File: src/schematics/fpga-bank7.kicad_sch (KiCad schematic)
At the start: 7 parts

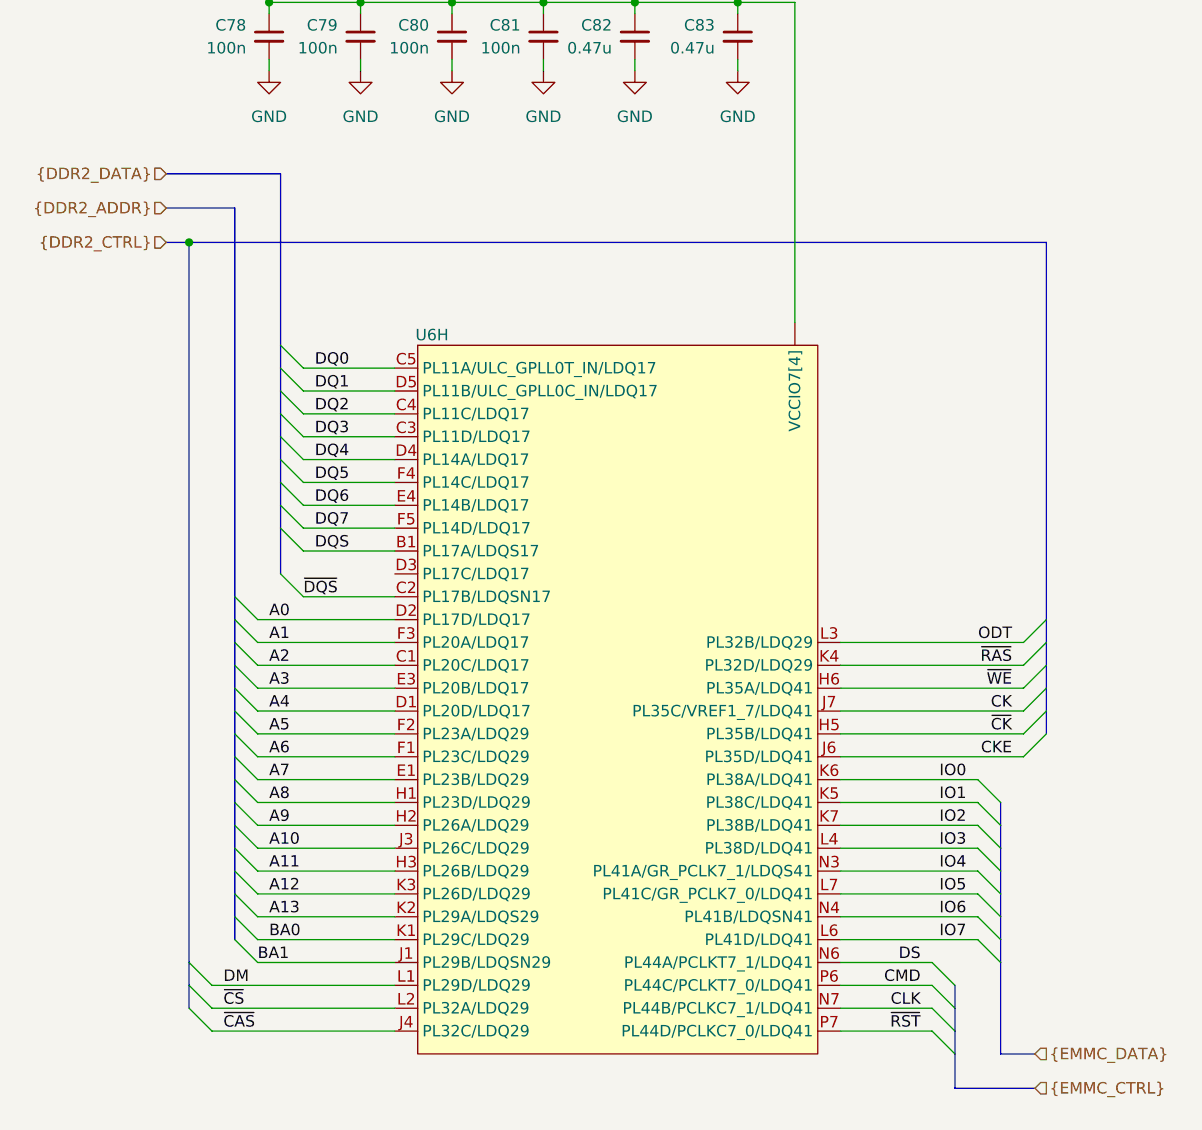
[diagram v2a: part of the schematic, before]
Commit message: Adds bus aliases
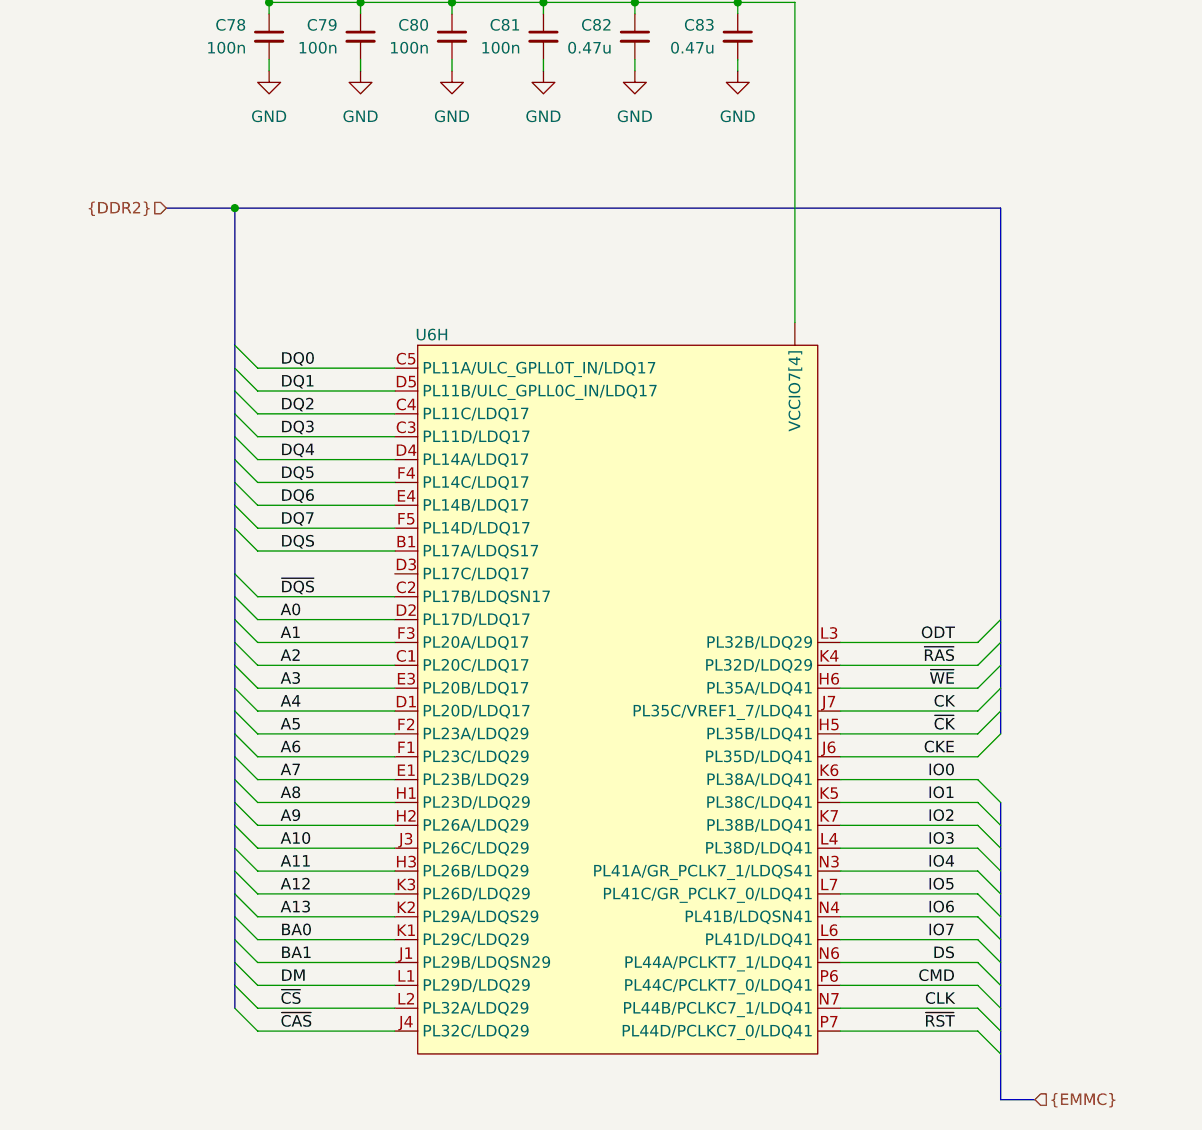
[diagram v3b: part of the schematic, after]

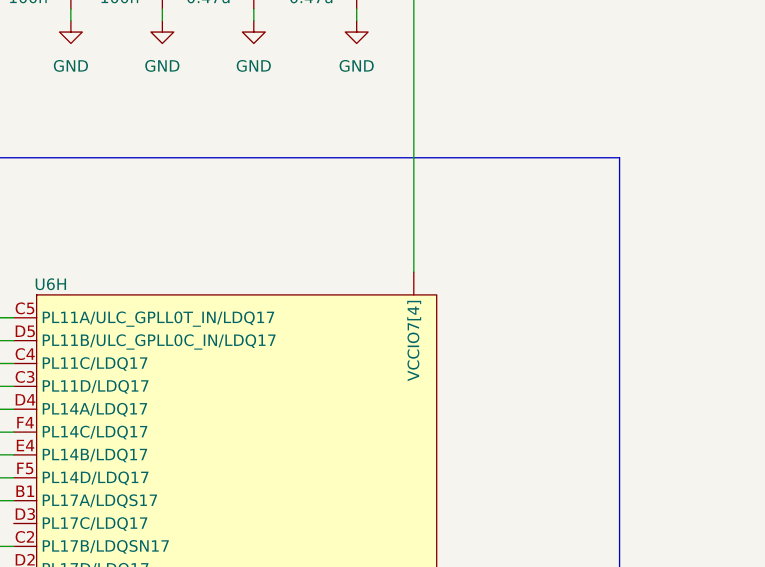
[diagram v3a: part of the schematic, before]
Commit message: Fix some ERC issues
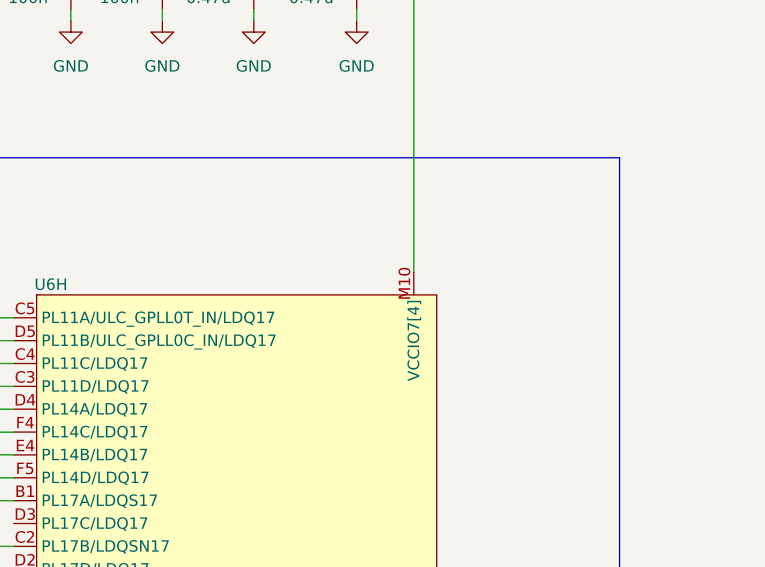
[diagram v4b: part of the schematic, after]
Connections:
- net +1V8: no longer U6. (VCCIO7[4])
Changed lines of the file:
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@@
 		(pin "Y31"
 		)
-		(pin ""
-		)
 		(pin "A10"
 		)
@@
 		(pin "Y32"
 		)
-		(pin ""
-		)
 		(pin "AB23"
 		)
@@
 		(pin "K16"
 		)
-		(pin ""
-		)
 		(pin "A18"
 		)
@@
 		(pin "K21"
 		)
-		(pin ""
-		)
 		(pin "B32"
 		)
@@
 		(pin "T23"
 		)
-		(pin ""
-		)
 		(pin "AA23"
 		)
@@
 		(pin "AM31"
 		)
-		(pin ""
-		)
 		(pin "AA10"
 		)
@@
 		(pin "Y7"
 		)
-		(pin ""
-		)
 		(pin "B1"
 		)
@@
 		(pin "T10"
 		)
-		(pin ""
-		)
 		(pin "AB10"
 		)
@@
 		(pin "M14"
 		)
-		(pin ""
-		)
 		(pin "AH12"
 		)
@@
 		(pin "V19"
 		)
-		(pin ""
-		)
 		(pin "AC11"
 		)
@@
 		(pin "AA11"
 		)
-		(pin ""
-		)
 		(instances

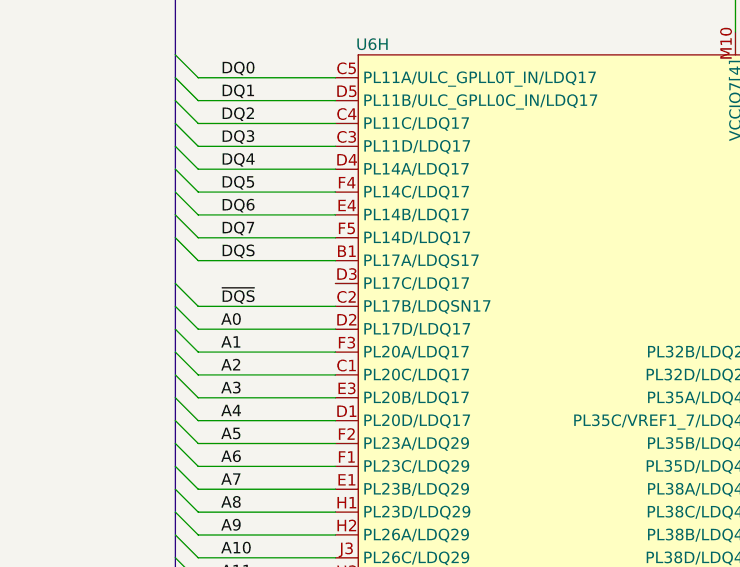
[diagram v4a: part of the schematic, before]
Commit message: Fixes bus aliases
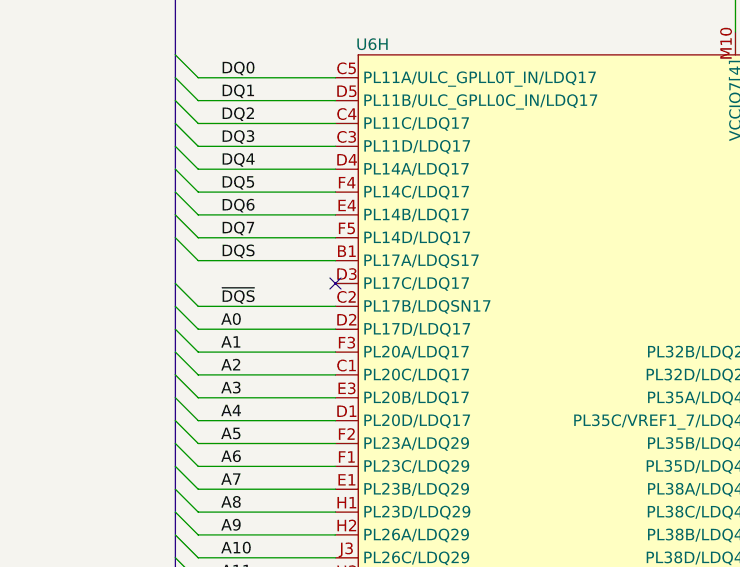
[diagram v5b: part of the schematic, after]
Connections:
- no-connect marks 0 -> 1
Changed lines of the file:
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@@
 		(color 0 0 0 0)
+	)
+	(no_connect
+		(at 127 96.52)
 	)
 	(bus_entry
@@
 		(pin "AB32"
 		)
-		(pin "AB32"
+		(pin "AB31"
 		)
 		(pin "AC26"

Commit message: Updates the root page
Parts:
- renumbered C78 to C72, C79 to C73, C80 to C74, C81 to C75, C82 to C76, C83 to C77
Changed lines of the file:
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@@
 		)
 	)
-	(hierarchical_label "{EMMC}"
+	(hierarchical_label "EMMC_~{RST}"
 		(shape input)
-		(at 198.12 154.94 0)
+		(at 22.86 82.55 180)
 		(fields_autoplaced yes)
 		(effects
@@
 				(size 1.27 1.27)
 			)
+			(justify right)
+		)
+	)
+	(hierarchical_label "EMMC_CLK"
+		(shape input)
+		(at 22.86 85.09 180)
+		(fields_autoplaced yes)
+		(effects
+			(font
+				(size 1.27 1.27)
+			)
+			(justify right)
+		)
+	)
+	(hierarchical_label "EMMC_DS"
+		(shape input)
+		(at 22.86 91.44 180)
+		(fields_autoplaced yes)
+		(effects
+			(font
+				(size 1.27 1.27)
+			)
+			(justify right)
+		)
+	)
+	(hierarchical_label "EMMC_IO[0..7]"
+		(shape input)
+		(at 20.32 97.79 0)
+		(fields_autoplaced yes)
+		(effects
+			(font
+				(size 1.27 1.27)
+			)
 			(justify left)
 		)
 	)
-	(hierarchical_label "{DDR2}"
+	(hierarchical_label "EMMC_CMD"
 		(shape input)
-		(at 101.6 55.88 180)
+		(at 22.86 88.9 180)
 		(fields_autoplaced yes)
 		(effects
@@
 		(dnp no)
 		(fields_autoplaced yes)
-		(property "Reference" "#PWR060"
+		(property "Reference" "#PWR053"
 			(at 113.03 33.02 0)
 			(effects
@@
 		(instances
 			(project "ecap5-bsom"
-				(path "/c5fd18a3-9aa0-4151-b6e0-94da3d606686/9ec64d27-698a-408d-bb9c-7e381193a80d/9a63a507-5244-41c3-8e77-e9299b12167a"
-					(reference "#PWR060")
+				(path "/c5fd18a3-9aa0-4151-b6e0-94da3d606686/f3fcc28f-f4b5-4b97-b1c8-620b151b8835"
+					(reference "#PWR053")
 					(unit 1)
 				)
@@
 		(dnp no)
 		(fields_autoplaced yes)
-		(property "Reference" "#PWR063"
+		(property "Reference" "#PWR056"
 			(at 133.35 46.99 0)
 			(effects
@@
 		(instances
 			(project "ecap5-bsom"
-				(path "/c5fd18a3-9aa0-4151-b6e0-94da3d606686/9ec64d27-698a-408d-bb9c-7e381193a80d/9a63a507-5244-41c3-8e77-e9299b12167a"
-					(reference "#PWR063")
+				(path "/c5fd18a3-9aa0-4151-b6e0-94da3d606686/f3fcc28f-f4b5-4b97-b1c8-620b151b8835"
+					(reference "#PWR056")
 					(unit 1)
 				)
@@
 		(dnp no)
 		(fields_autoplaced yes)
-		(property "Reference" "C83"
+		(property "Reference" "C77"
 			(at 162.56 35.5662 0)
 			(effects
@@
 		(instances
 			(project "ecap5-bsom"
-				(path "/c5fd18a3-9aa0-4151-b6e0-94da3d606686/9ec64d27-698a-408d-bb9c-7e381193a80d/9a63a507-5244-41c3-8e77-e9299b12167a"
-					(reference "C83")
+				(path "/c5fd18a3-9aa0-4151-b6e0-94da3d606686/f3fcc28f-f4b5-4b97-b1c8-620b151b8835"
+					(reference "C77")
 					(unit 1)
 				)
@@
 		(dnp no)
 		(fields_autoplaced yes)
-		(property "Reference" "#PWR062"
+		(property "Reference" "#PWR055"
 			(at 123.19 46.99 0)
 			(effects
@@
 		(instances
 			(project "ecap5-bsom"
-				(path "/c5fd18a3-9aa0-4151-b6e0-94da3d606686/9ec64d27-698a-408d-bb9c-7e381193a80d/9a63a507-5244-41c3-8e77-e9299b12167a"
-					(reference "#PWR062")
+				(path "/c5fd18a3-9aa0-4151-b6e0-94da3d606686/f3fcc28f-f4b5-4b97-b1c8-620b151b8835"
+					(reference "#PWR055")
 					(unit 1)
 				)
@@
 		(dnp no)
 		(fields_autoplaced yes)
-		(property "Reference" "#PWR064"
+		(property "Reference" "#PWR057"
 			(at 143.51 46.99 0)
 			(effects
@@
 		(instances
 			(project "ecap5-bsom"
-				(path "/c5fd18a3-9aa0-4151-b6e0-94da3d606686/9ec64d27-698a-408d-bb9c-7e381193a80d/9a63a507-5244-41c3-8e77-e9299b12167a"
-					(reference "#PWR064")
+				(path "/c5fd18a3-9aa0-4151-b6e0-94da3d606686/f3fcc28f-f4b5-4b97-b1c8-620b151b8835"
+					(reference "#PWR057")
 					(unit 1)
 				)
@@
 		(dnp no)
 		(fields_autoplaced yes)
-		(property "Reference" "#PWR061"
+		(property "Reference" "#PWR054"
 			(at 113.03 46.99 0)
 			(effects
@@
 		(instances
 			(project "ecap5-bsom"
-				(path "/c5fd18a3-9aa0-4151-b6e0-94da3d606686/9ec64d27-698a-408d-bb9c-7e381193a80d/9a63a507-5244-41c3-8e77-e9299b12167a"
-					(reference "#PWR061")
+				(path "/c5fd18a3-9aa0-4151-b6e0-94da3d606686/f3fcc28f-f4b5-4b97-b1c8-620b151b8835"
+					(reference "#PWR054")
 					(unit 1)
 				)
@@
 		(instances
 			(project "ecap5-bsom"
-				(path "/c5fd18a3-9aa0-4151-b6e0-94da3d606686/9ec64d27-698a-408d-bb9c-7e381193a80d/9a63a507-5244-41c3-8e77-e9299b12167a"
+				(path "/c5fd18a3-9aa0-4151-b6e0-94da3d606686/f3fcc28f-f4b5-4b97-b1c8-620b151b8835"
 					(reference "U6")
 					(unit 8)
@@
 		(dnp no)
 		(fields_autoplaced yes)
-		(property "Reference" "C82"
+		(property "Reference" "C76"
 			(at 151.13 35.5662 0)
 			(effects
@@
 		(instances
 			(project "ecap5-bsom"
-				(path "/c5fd18a3-9aa0-4151-b6e0-94da3d606686/9ec64d27-698a-408d-bb9c-7e381193a80d/9a63a507-5244-41c3-8e77-e9299b12167a"
-					(reference "C82")
+				(path "/c5fd18a3-9aa0-4151-b6e0-94da3d606686/f3fcc28f-f4b5-4b97-b1c8-620b151b8835"
+					(reference "C76")
 					(unit 1)
 				)
@@
 		(dnp no)
 		(fields_autoplaced yes)
-		(property "Reference" "#PWR066"
+		(property "Reference" "#PWR059"
 			(at 165.1 46.99 0)
 			(effects
@@
 		(instances
 			(project "ecap5-bsom"
-				(path "/c5fd18a3-9aa0-4151-b6e0-94da3d606686/9ec64d27-698a-408d-bb9c-7e381193a80d/9a63a507-5244-41c3-8e77-e9299b12167a"
-					(reference "#PWR066")
+				(path "/c5fd18a3-9aa0-4151-b6e0-94da3d606686/f3fcc28f-f4b5-4b97-b1c8-620b151b8835"
+					(reference "#PWR059")
 					(unit 1)
 				)
@@
 		(dnp no)
 		(fields_autoplaced yes)
-		(property "Reference" "C79"
+		(property "Reference" "C73"
 			(at 120.65 35.5662 0)
 			(effects
@@
 		(instances
 			(project "ecap5-bsom"
-				(path "/c5fd18a3-9aa0-4151-b6e0-94da3d606686/9ec64d27-698a-408d-bb9c-7e381193a80d/9a63a507-5244-41c3-8e77-e9299b12167a"
-					(reference "C79")
+				(path "/c5fd18a3-9aa0-4151-b6e0-94da3d606686/f3fcc28f-f4b5-4b97-b1c8-620b151b8835"
+					(reference "C73")
 					(unit 1)
 				)
@@
 		(dnp no)
 		(fields_autoplaced yes)
-		(property "Reference" "C80"
+		(property "Reference" "C74"
 			(at 130.81 35.5662 0)
 			(effects
@@
 		(instances
 			(project "ecap5-bsom"
-				(path "/c5fd18a3-9aa0-4151-b6e0-94da3d606686/9ec64d27-698a-408d-bb9c-7e381193a80d/9a63a507-5244-41c3-8e77-e9299b12167a"
-					(reference "C80")
+				(path "/c5fd18a3-9aa0-4151-b6e0-94da3d606686/f3fcc28f-f4b5-4b97-b1c8-620b151b8835"
+					(reference "C74")
 					(unit 1)
 				)
@@
 		(dnp no)
 		(fields_autoplaced yes)
-		(property "Reference" "#PWR065"
+		(property "Reference" "#PWR058"
 			(at 153.67 46.99 0)
 			(effects
@@
 		(instances
 			(project "ecap5-bsom"
-				(path "/c5fd18a3-9aa0-4151-b6e0-94da3d606686/9ec64d27-698a-408d-bb9c-7e381193a80d/9a63a507-5244-41c3-8e77-e9299b12167a"
-					(reference "#PWR065")
+				(path "/c5fd18a3-9aa0-4151-b6e0-94da3d606686/f3fcc28f-f4b5-4b97-b1c8-620b151b8835"
+					(reference "#PWR058")
 					(unit 1)
 				)
@@
 		(dnp no)
 		(fields_autoplaced yes)
-		(property "Reference" "C78"
+		(property "Reference" "C72"
 			(at 110.49 35.5662 0)
 			(effects
@@
 		(instances
 			(project "ecap5-bsom"
-				(path "/c5fd18a3-9aa0-4151-b6e0-94da3d606686/9ec64d27-698a-408d-bb9c-7e381193a80d/9a63a507-5244-41c3-8e77-e9299b12167a"
-					(reference "C78")
+				(path "/c5fd18a3-9aa0-4151-b6e0-94da3d606686/f3fcc28f-f4b5-4b97-b1c8-620b151b8835"
+					(reference "C72")
 					(unit 1)
 				)
@@
 		(dnp no)
 		(fields_autoplaced yes)
-		(property "Reference" "C81"
+		(property "Reference" "C75"
 			(at 140.97 35.5662 0)
 			(effects
@@
 		(instances
 			(project "ecap5-bsom"
-				(path "/c5fd18a3-9aa0-4151-b6e0-94da3d606686/9ec64d27-698a-408d-bb9c-7e381193a80d/9a63a507-5244-41c3-8e77-e9299b12167a"
-					(reference "C81")
+				(path "/c5fd18a3-9aa0-4151-b6e0-94da3d606686/f3fcc28f-f4b5-4b97-b1c8-620b151b8835"
+					(reference "C75")
 					(unit 1)
 				)

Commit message: Finishes the root page
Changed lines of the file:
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@@
 		)
 	)
-	(hierarchical_label "EMMC_~{RST}"
+	(hierarchical_label "DDR2.DM"
+		(shape input)
+		(at 31.75 156.21 0)
+		(fields_autoplaced yes)
+		(effects
+			(font
+				(size 1.27 1.27)
+			)
+			(justify left)
+		)
+	)
+	(hierarchical_label "DDR2.CKE"
+		(shape input)
+		(at 41.91 184.15 180)
+		(fields_autoplaced yes)
+		(effects
+			(font
+				(size 1.27 1.27)
+			)
+			(justify right)
+		)
+	)
+	(hierarchical_label "DDR2.CK"
+		(shape input)
+		(at 41.91 179.07 180)
+		(fields_autoplaced yes)
+		(effects
+			(font
+				(size 1.27 1.27)
+			)
+			(justify right)
+		)
+	)
+	(hierarchical_label "EMMC.~{RST}"
 		(shape input)
 		(at 22.86 82.55 180)
@@
 		)
 	)
-	(hierarchical_label "EMMC_CLK"
+	(hierarchical_label "DDR2.~{CAS}"
+		(shape input)
+		(at 31.75 151.13 0)
+		(fields_autoplaced yes)
+		(effects
+			(font
+				(size 1.27 1.27)
+			)
+			(justify left)
+		)
+	)
+	(hierarchical_label "DDR2.~{WE}"
+		(shape input)
+		(at 31.75 143.51 0)
+		(fields_autoplaced yes)
+		(effects
+			(font
+				(size 1.27 1.27)
+			)
+			(justify left)
+		)
+	)
+	(hierarchical_label "DDR2.~{CK}"
+		(shape input)
+		(at 41.91 181.61 180)
+		(fields_autoplaced yes)
+		(effects
+			(font
+				(size 1.27 1.27)
+			)
+			(justify right)
+		)
+	)
+	(hierarchical_label "DDR2.~{CS}"
+		(shape input)
+		(at 31.75 153.67 0)
+		(fields_autoplaced yes)
+		(effects
+			(font
+				(size 1.27 1.27)
+			)
+			(justify left)
+		)
+	)
+	(hierarchical_label "DDR2.ODT"
+		(shape input)
+		(at 31.75 148.59 0)
+		(fields_autoplaced yes)
+		(effects
+			(font
+				(size 1.27 1.27)
+			)
+			(justify left)
+		)
+	)
+	(hierarchical_label "DDR2.~{RAS}"
+		(shape input)
+		(at 31.75 146.05 0)
+		(fields_autoplaced yes)
+		(effects
+			(font
+				(size 1.27 1.27)
+			)
+			(justify left)
+		)
+	)
+	(hierarchical_label "DDR2.BA[0..1]"
+		(shape input)
+		(at 38.1 166.37 180)
+		(fields_autoplaced yes)
+		(effects
+			(font
+				(size 1.27 1.27)
+			)
+			(justify right)
+		)
+	)
+	(hierarchical_label "DDR2.A[0..13]"
+		(shape input)
+		(at 38.1 128.27 180)
+		(fields_autoplaced yes)
+		(effects
+			(font
+				(size 1.27 1.27)
+			)
+			(justify right)
+		)
+	)
+	(hierarchical_label "EMMC.CLK"
 		(shape input)
 		(at 22.86 85.09 180)
@@
 		)
 	)
-	(hierarchical_label "EMMC_DS"
+	(hierarchical_label "DDR2.DQS"
+		(shape input)
+		(at 31.75 135.89 0)
+		(fields_autoplaced yes)
+		(effects
+			(font
+				(size 1.27 1.27)
+			)
+			(justify left)
+		)
+	)
+	(hierarchical_label "EMMC.DS"
 		(shape input)
 		(at 22.86 91.44 180)
@@
 		)
 	)
-	(hierarchical_label "EMMC_IO[0..7]"
+	(hierarchical_label "EMMC.IO[0..7]"
 		(shape input)
 		(at 20.32 97.79 0)
@@
 		)
 	)
-	(hierarchical_label "EMMC_CMD"
+	(hierarchical_label "DDR2.DQ[0..7]"
+		(shape input)
+		(at 50.8 137.16 0)
+		(fields_autoplaced yes)
+		(effects
+			(font
+				(size 1.27 1.27)
+			)
+			(justify left)
+		)
+	)
+	(hierarchical_label "EMMC.CMD"
 		(shape input)
 		(at 22.86 88.9 180)
@@
 		)
 	)
+	(hierarchical_label "DDR2.~{DQS}"
+		(shape input)
+		(at 31.75 138.43 0)
+		(fields_autoplaced yes)
+		(effects
+			(font
+				(size 1.27 1.27)
+			)
+			(justify left)
+		)
+	)
